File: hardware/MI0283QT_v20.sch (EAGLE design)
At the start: 52 parts, among them Q1 16MHz, T1 N-CHN, U1 TS5204-3V3, X1 PASSER, X2 PASSER, X3 PASSER, X4 PASSER

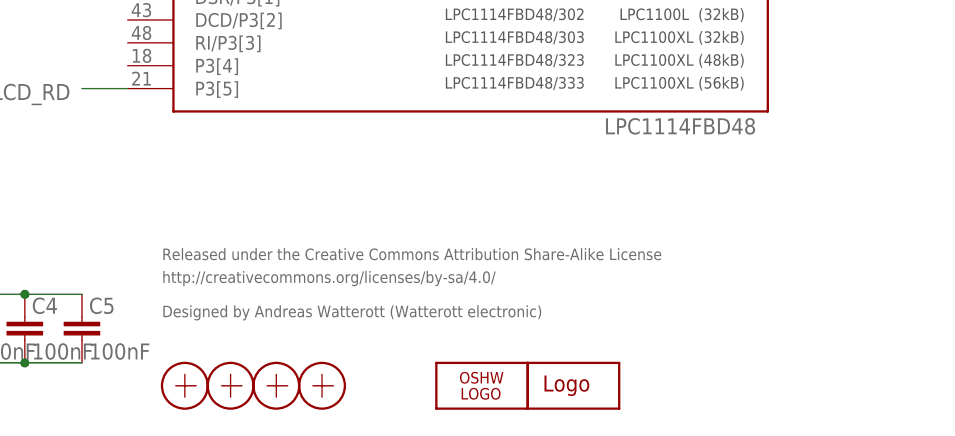
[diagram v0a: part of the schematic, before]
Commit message: updated schematics
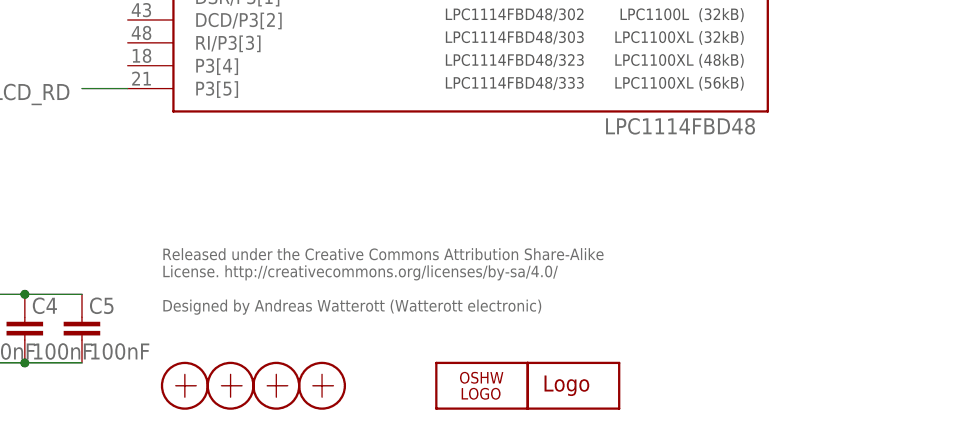
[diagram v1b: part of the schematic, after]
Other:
- note added: "Released under the Creative Commons Attribution Share-Alike License. http://creativecommons.org/licenses/by-sa/4.0/ Designed by Andreas Watterott (Watterott electronic)"
- note removed: "Designed by Andreas Watterott (Watterott electronic)"
- note removed: "Released under the Creative Commons Attribution Share-Alike License"
- note removed: "http://creativecommons.org/licenses/by-sa/4.0/"
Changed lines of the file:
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@@
 <?xml version="1.0" encoding="utf-8"?>
 <!DOCTYPE eagle SYSTEM "eagle.dtd">
-<eagle version="6.6.0">
+<eagle version="7.5.0">
 <drawing>
 <settings>
@@
 <layer number="51" name="tDocu" color="7" fill="1" visible="no" active="no"/>
 <layer number="52" name="bDocu" color="7" fill="1" visible="no" active="no"/>
-<layer number="53" name="tCopper" color="7" fill="11" visible="no" active="no"/>
-<layer number="54" name="bCopper" color="7" fill="1" visible="no" active="no"/>
-<layer number="56" name="wert" color="7" fill="1" visible="no" active="no"/>
 <layer number="91" name="Nets" color="2" fill="1" visible="yes" active="yes"/>
 <layer number="92" name="Busses" color="1" fill="1" visible="yes" active="yes"/>
@@
 <layer number="97" name="Info" color="7" fill="1" visible="yes" active="yes"/>
 <layer number="98" name="Guide" color="6" fill="1" visible="yes" active="yes"/>
-<layer number="100" name="Muster" color="7" fill="1" visible="no" active="no"/>
 <layer number="250" name="Descript" color="3" fill="1" visible="yes" active="yes"/>
-<layer number="251" name="SMDround" color="12" fill="11" visible="no" active="no"/>
 </layers>
 <schematic xreflabel="%F%N/%S.%C%R" xrefpart="/%S.%C%R">
@@
 <text x="38.735" y="146.685" size="1.778" layer="95">0</text>
 <text x="38.735" y="139.065" size="1.778" layer="95">0</text>
-<text x="162.56" y="21.59" size="1.27" layer="95">Released under the Creative Commons Attribution Share-Alike License</text>
-<text x="162.56" y="19.05" size="1.27" layer="95">http://creativecommons.org/licenses/by-sa/4.0/</text>
-<text x="162.56" y="15.24" size="1.27" layer="95">Designed by Andreas Watterott (Watterott electronic)</text>
+<text x="162.56" y="22.86" size="1.27" layer="95" align="top-left">Released under the Creative Commons Attribution Share-Alike
+License. http://creativecommons.org/licenses/by-sa/4.0/
+Designed by Andreas Watterott (Watterott electronic)</text>
 <text x="21.59" y="166.37" size="3.81" layer="250">Display with Touch-Panel</text>
 <text x="179.07" y="166.37" size="3.81" layer="250">ARM Cortex-M0</text>
@@
 </schematic>
 </drawing>
+<compatibility>
+<note version="6.3" minversion="6.2.2" severity="warning">
+Since Version 6.2.2 text objects can contain more than one line,
+which will not be processed correctly with this version.
+</note>
+</compatibility>
 </eagle>

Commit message: updated PDFs and schematics
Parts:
- R1, R2, R3, R4, R5: value 22 -> 47
- R10, R7, R8, R9: value 22 -> 0
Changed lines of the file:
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@@
 <?xml version="1.0" encoding="utf-8"?>
 <!DOCTYPE eagle SYSTEM "eagle.dtd">
-<eagle version="7.5.0">
+<eagle version="7.7.0">
 <drawing>
 <settings>
@@
 <setting verticaltext="up"/>
 </settings>
-<grid distance="0.05" unitdist="inch" unit="inch" style="lines" multiple="1" display="yes" altdistance="0.025" altunitdist="inch" altunit="inch"/>
+<grid distance="0.1" unitdist="inch" unit="inch" style="lines" multiple="1" display="no" altdistance="0.01" altunitdist="inch" altunit="inch"/>
 <layers>
 <layer number="1" name="Top" color="4" fill="1" visible="no" active="no"/>
@@
 <parts>
 <part name="GND3" library="supply1" deviceset="GND" device=""/>
-<part name="R1" library="rcl" deviceset="R-EU_" device="R0603" value="22"/>
-<part name="R2" library="rcl" deviceset="R-EU_" device="R0603" value="22"/>
-<part name="R3" library="rcl" deviceset="R-EU_" device="R0603" value="22"/>
-<part name="R4" library="rcl" deviceset="R-EU_" device="R0603" value="22"/>
+<part name="R1" library="rcl" deviceset="R-EU_" device="R0603" value="47"/>
+<part name="R2" library="rcl" deviceset="R-EU_" device="R0603" value="47"/>
+<part name="R3" library="rcl" deviceset="R-EU_" device="R0603" value="47"/>
+<part name="R4" library="rcl" deviceset="R-EU_" device="R0603" value="47"/>
 <part name="U1" library="Voltage-Reg" deviceset="TS5204" device="" value="TS5204-3V3"/>
 <part name="GND9" library="supply1" deviceset="GND" device=""/>
@@
 <part name="C4" library="rcl" deviceset="C-EU" device="C0603" value="100nF"/>
 <part name="C5" library="rcl" deviceset="C-EU" device="C0603" value="100nF"/>
-<part name="R5" library="rcl" deviceset="R-EU_" device="R0603" value="22"/>
+<part name="R5" library="rcl" deviceset="R-EU_" device="R0603" value="47"/>
 <part name="P+1" library="supply1" deviceset="VCC" device=""/>
 <part name="GND7" library="supply1" deviceset="GND" device=""/>
@@
 <part name="GND10" library="supply1" deviceset="GND" device=""/>
 <part name="P+5" library="supply1" deviceset="VCC" device=""/>
-<part name="R7" library="rcl" deviceset="R-EU_" device="R0603" value="22"/>
-<part name="R8" library="rcl" deviceset="R-EU_" device="R0603" value="22"/>
-<part name="R9" library="rcl" deviceset="R-EU_" device="R0603" value="22"/>
-<part name="R10" library="rcl" deviceset="R-EU_" device="R0603" value="22"/>
+<part name="R7" library="rcl" deviceset="R-EU_" device="R0603" value="0"/>
+<part name="R8" library="rcl" deviceset="R-EU_" device="R0603" value="0"/>
+<part name="R9" library="rcl" deviceset="R-EU_" device="R0603" value="0"/>
+<part name="R10" library="rcl" deviceset="R-EU_" device="R0603" value="0"/>
 <part name="6-DTR" library="wirepad" deviceset="WIREPAD" device="SMD1,27-254"/>
 <part name="5-RXI" library="wirepad" deviceset="WIREPAD" device="SMD1,27-254"/>
